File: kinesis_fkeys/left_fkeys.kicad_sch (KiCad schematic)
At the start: 10 parts, among them J2 LEFT_13_TOP

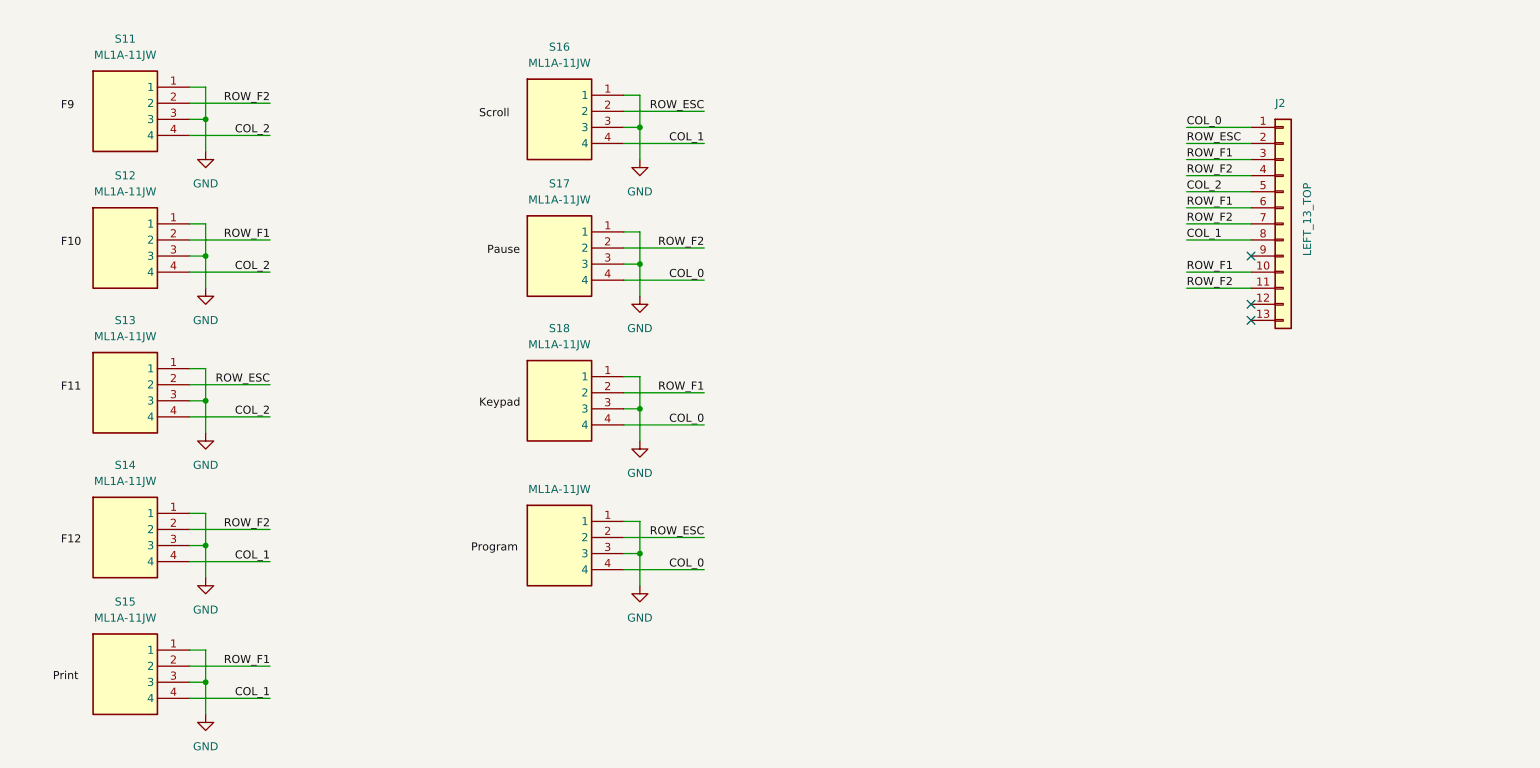
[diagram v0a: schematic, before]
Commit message: buttons schematics verified and placed on the pcb on exact spots
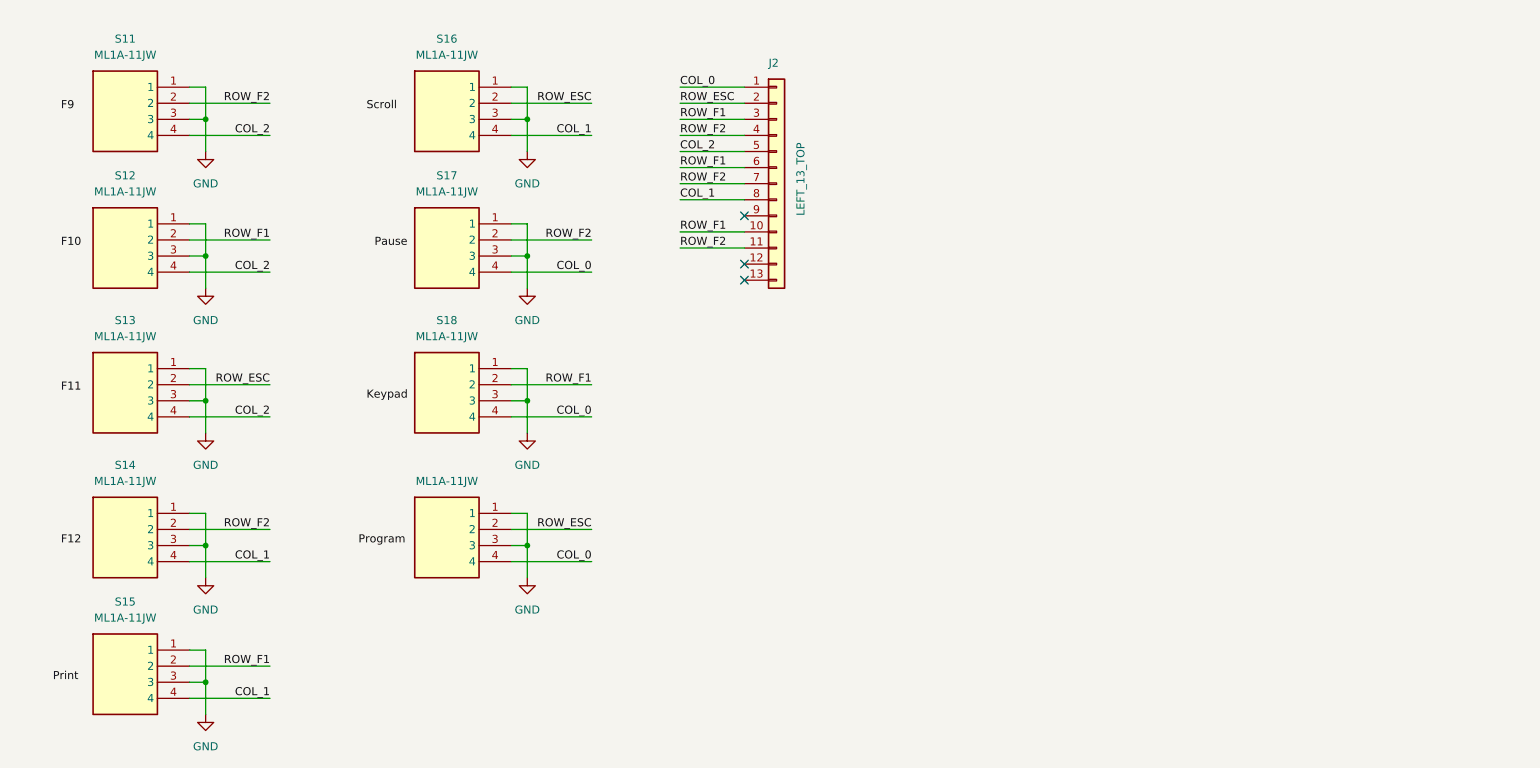
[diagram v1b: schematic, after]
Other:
- moved on the sheet: J2, S16, S17, S18

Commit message: added diods againts ghosting on the both PCBs
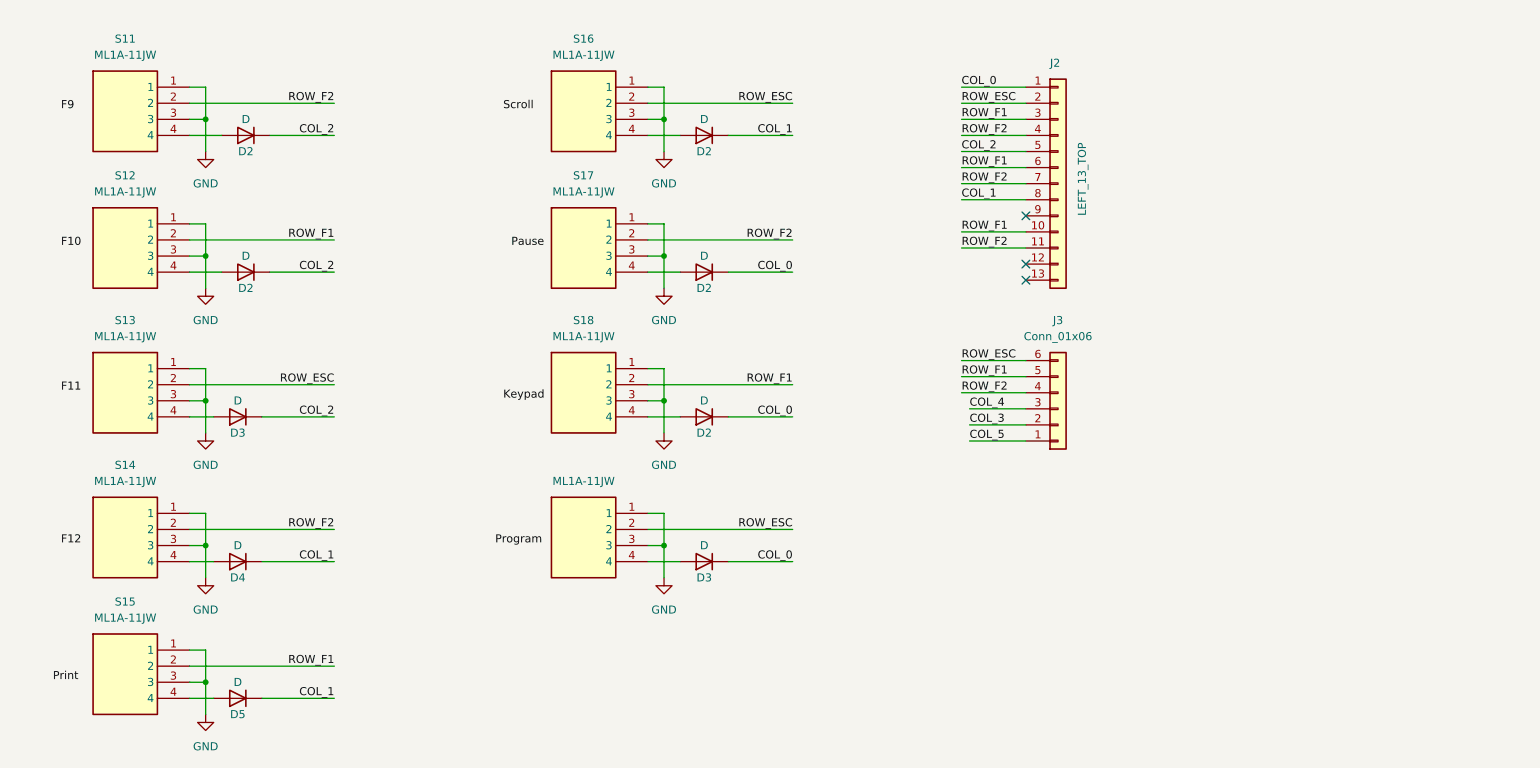
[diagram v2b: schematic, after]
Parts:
- added D2 (x5), D3 (x2), D4, D5: D, Diode_SMD:D_MiniMELF_Handsoldering, symbol Device:D
- added J3: Conn_01x06, symbol Connector_Generic:Conn_01x06
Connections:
- net COL_0: now also D2.1 (K), D2.1 (K), D3.1 (K); no longer S10.4, S17.4, S18.4
- net COL_1: now also D2.1 (K), D4.1 (K), D5.1 (K); no longer S14.4, S15.4, S16.4
- net COL_2: now also D2.1 (K), D2.1 (K), D3.1 (K); no longer S11.4, S12.4, S13.4
- net ROW_ESC: now also J3.6 (Pin_6)
- net ROW_F1: now also J3.5 (Pin_5)
- net ROW_F2: now also J3.4 (Pin_4)
- new net: D5.2 (A), S15.4
- new net: D2.2 (A), S17.4
- new net: D4.2 (A), S14.4
- new net: D3.2 (A), S13.4
- new net: D2.2 (A), S16.4
- new net: D2.2 (A), S11.4
- new net: D2.2 (A), S12.4
- new net: D2.2 (A), S18.4
- new net: D3.2 (A), S10.4
- new net COL_3: J3.2 (Pin_2)
- new net COL_4: J3.3 (Pin_3)
- new net COL_5: J3.1 (Pin_1)
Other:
- moved on the sheet: J2, S16, S17, S18

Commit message: added TE 84953 6 pin connectors to reduce amount of tracks
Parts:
- J3: footprint (none) -> dodo_conn:84953-6
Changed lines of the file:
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@@
       (effects (font (size 1.27 1.27)))
     )
-    (property "Footprint" "" (at 200.66 87.63 0)
+    (property "Footprint" "dodo_conn:84953-6" (at 200.66 87.63 0)
       (effects (font (size 1.27 1.27)) hide)
     )

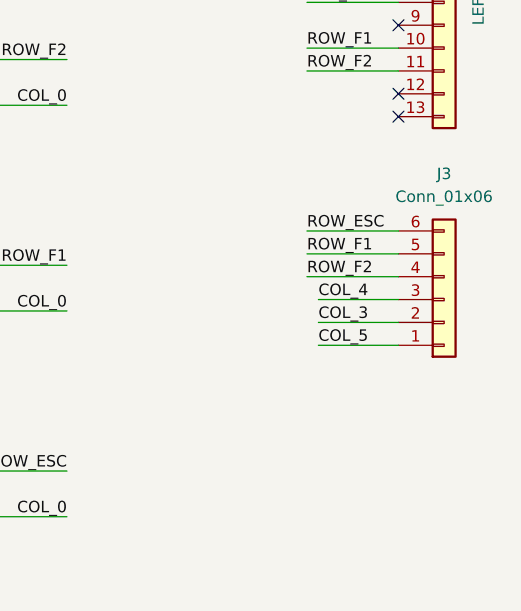
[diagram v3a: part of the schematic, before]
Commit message: fixed wrong amount pins on the footprint and sorted pinout on the connectors
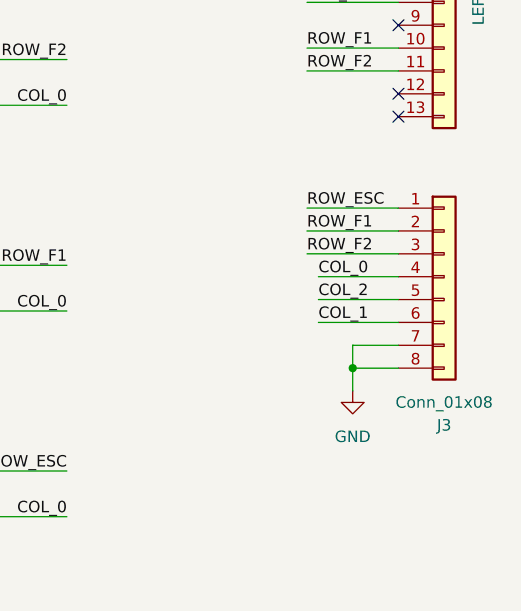
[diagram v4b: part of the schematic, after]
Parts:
- removed J3: Conn_01x06, dodo_conn:84953-6, symbol Connector_Generic:Conn_01x06
- added J3: Conn_01x08, dodo_conn:84953-6, symbol Connector_Generic:Conn_01x08
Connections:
- net COL_0: now also J3.4 (Pin_4)
- net COL_1: now also J3.6 (Pin_6)
- net COL_2: now also J3.5 (Pin_5)
- net GND: now also J3.7 (Pin_7), J3.8 (Pin_8)
- net ROW_ESC: now also J3.1 (Pin_1)
- net ROW_F1: now also J3.2 (Pin_2)
- net ROW_F2: now also J3.3 (Pin_3)
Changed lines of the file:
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@@
   (junction (at 66.04 41.91) (diameter 0) (color 0 0 0 0)
+  )
+  (junction (at 190.5 95.25) (diameter 0) (color 0 0 0 0)
   )
   (junction (at 66.04 63.5) (diameter 0) (color 0 0 0 0)
@@
     (stroke (width 0) (type default))
   )
+  (wire (pts (xy 185.42 80.01) (xy 195.58 80.01))
+    (stroke (width 0) (type default))
+  )
   (wire (pts (xy 66.04 36.83) (xy 66.04 41.91))
     (stroke (width 0) (type default))
@@
     (stroke (width 0) (type default))
   )
+  (wire (pts (xy 186.69 90.17) (xy 195.58 90.17))
+    (stroke (width 0) (type default))
+  )
   (wire (pts (xy 138.43 81.28) (xy 138.43 86.36))
     (stroke (width 0) (type default))
@@
     (stroke (width 0) (type default))
   )
+  (wire (pts (xy 190.5 95.25) (xy 190.5 97.79))
+    (stroke (width 0) (type default))
+  )
   (wire (pts (xy 66.04 41.91) (xy 66.04 46.99))
     (stroke (width 0) (type default))
@@
     (stroke (width 0) (type default))
   )
+  (wire (pts (xy 186.69 85.09) (xy 195.58 85.09))
+    (stroke (width 0) (type default))
+  )
   (wire (pts (xy 138.43 86.36) (xy 138.43 91.44))
     (stroke (width 0) (type default))
@@
     (stroke (width 0) (type default))
   )
+  (wire (pts (xy 190.5 92.71) (xy 190.5 95.25))
+    (stroke (width 0) (type default))
+  )
   (wire (pts (xy 135.89 88.9) (xy 140.97 88.9))
     (stroke (width 0) (type default))
@@
     (stroke (width 0) (type default))
   )
-  (wire (pts (xy 195.58 92.71) (xy 186.69 92.71))
-    (stroke (width 0) (type default))
-  )
   (wire (pts (xy 138.43 63.5) (xy 138.43 68.58))
     (stroke (width 0) (type default))
@@
     (stroke (width 0) (type default))
   )
-  (wire (pts (xy 195.58 82.55) (xy 185.42 82.55))
-    (stroke (width 0) (type default))
-  )
   (wire (pts (xy 63.5 41.91) (xy 66.04 41.91))
     (stroke (width 0) (type default))
   )
+  (wire (pts (xy 185.42 77.47) (xy 195.58 77.47))
+    (stroke (width 0) (type default))
+  )
   (wire (pts (xy 148.59 66.04) (xy 158.75 66.04))
     (stroke (width 0) (type default))
@@
     (stroke (width 0) (type default))
   )
-  (wire (pts (xy 195.58 87.63) (xy 186.69 87.63))
-    (stroke (width 0) (type default))
-  )
   (wire (pts (xy 63.5 44.45) (xy 68.58 44.45))
     (stroke (width 0) (type default))
@@
     (stroke (width 0) (type default))
   )
-  (wire (pts (xy 195.58 80.01) (xy 185.42 80.01))
-    (stroke (width 0) (type default))
-  )
   (wire (pts (xy 63.5 104.14) (xy 66.04 104.14))
     (stroke (width 0) (type default))
   )
+  (wire (pts (xy 195.58 92.71) (xy 190.5 92.71))
+    (stroke (width 0) (type default))
+  )
   (wire (pts (xy 135.89 81.28) (xy 138.43 81.28))
     (stroke (width 0) (type default))
@@
     (stroke (width 0) (type default))
   )
-  (wire (pts (xy 195.58 90.17) (xy 186.69 90.17))
+  (wire (pts (xy 185.42 82.55) (xy 195.58 82.55))
     (stroke (width 0) (type default))
   )
@@
     (stroke (width 0) (type default))
   )
-  (wire (pts (xy 195.58 85.09) (xy 185.42 85.09))
-    (stroke (width 0) (type default))
-  )
   (wire (pts (xy 135.89 111.76) (xy 140.97 111.76))
     (stroke (width 0) (type default))
@@
     (stroke (width 0) (type default))
   )
+  (wire (pts (xy 195.58 95.25) (xy 190.5 95.25))
+    (stroke (width 0) (type default))
+  )
+  (wire (pts (xy 186.69 87.63) (xy 195.58 87.63))
+    (stroke (width 0) (type default))
+  )
   (wire (pts (xy 138.43 41.91) (xy 138.43 46.99))
     (stroke (width 0) (type default))
@@
     (effects (font (size 1.27 1.27)) (justify right bottom))
   )
-  (label "COL_5" (at 186.69 92.71 0) (fields_autoplaced)
+  (label "COL_1" (at 186.69 90.17 0) (fields_autoplaced)
     (effects (font (size 1.27 1.27)) (justify left bottom))
   )
@@
     (effects (font (size 1.27 1.27)) (justify left bottom))
   )
-  (label "ROW_F2" (at 185.42 85.09 0) (fields_autoplaced)
+  (label "ROW_F2" (at 185.42 82.55 0) (fields_autoplaced)
     (effects (font (size 1.27 1.27)) (justify left bottom))
   )
@@
     (effects (font (size 1.27 1.27)) (justify right bottom))
   )
-  (label "COL_3" (at 186.69 90.17 0) (fields_autoplaced)
+  (label "COL_2" (at 186.69 87.63 0) (fields_autoplaced)
     (effects (font (size 1.27 1.27)) (justify left bottom))
   )
@@
     (effects (font (size 1.27 1.27)) (justify left bottom))
   )
-  (label "ROW_F1" (at 185.42 82.55 0) (fields_autoplaced)
+  (label "ROW_F1" (at 185.42 80.01 0) (fields_autoplaced)
     (effects (font (size 1.27 1.27)) (justify left bottom))
   )
@@
     (effects (font (size 1.27 1.27)) (justify left bottom))
   )
-  (label "COL_4" (at 186.69 87.63 0) (fields_autoplaced)
-    (effects (font (size 1.27 1.27)) (justify left bottom))
-  )
-  (label "ROW_ESC" (at 185.42 80.01 0) (fields_autoplaced)
+  (label "COL_0" (at 186.69 85.09 0) (fields_autoplaced)
+    (effects (font (size 1.27 1.27)) (justify left bottom))
+  )
+  (label "ROW_ESC" (at 185.42 77.47 0) (fields_autoplaced)
     (effects (font (size 1.27 1.27)) (justify left bottom))
   )
@@
         (path "/06886ccb-17ec-482e-a853-bf4276494c0a/d08dcb93-9608-43f8-96f0-931b8e1132a9"
           (reference "D10") (unit 1)
-        )
-      )
-    )
-  )
-  (symbol (lib_id "Connector_Generic:Conn_01x06") (at 200.66 87.63 0) (mirror x) (unit 1)
-    (exclude_from_sim no) (in_bom yes) (on_board yes) (dnp no) (fields_autoplaced)
-    (property "Reference" "J3" (at 200.66 73.66 0)
-      (effects (font (size 1.27 1.27)))
-    )
-    (property "Value" "Conn_01x06" (at 200.66 76.2 0)
-      (effects (font (size 1.27 1.27)))
-    )
-    (property "Footprint" "dodo_conn:84953-6" (at 200.66 87.63 0)
-      (effects (font (size 1.27 1.27)) hide)
-    )
-    (property "Datasheet" "~" (at 200.66 87.63 0)
-      (effects (font (size 1.27 1.27)) hide)
-    )
-    (property "Description" "Generic connector, single row, 01x06, script generated (kicad-library-utils/schlib/autogen/connector/)" (at 200.66 87.63 0)
-      (effects (font (size 1.27 1.27)) hide)
-    )
-    (pin "6")
-    (pin "1")
-    (pin "2")
-    (pin "5")
-    (pin "3")
-    (pin "4")
-    (instances
-      (project "kinesis_fkeys"
-        (path "/06886ccb-17ec-482e-a853-bf4276494c0a/106b8080-7c92-4036-9b29-d3ff48894255"
-          (reference "J3") (unit 1)
-        )
-        (path "/06886ccb-17ec-482e-a853-bf4276494c0a/d08dcb93-9608-43f8-96f0-931b8e1132a9"
-          (reference "J4") (unit 1)
         )
       )
@@
     )
   )
+  (symbol (lib_id "power:GND") (at 190.5 97.79 0) (mirror y) (unit 1)
+    (exclude_from_sim no) (in_bom yes) (on_board yes) (dnp no) (fields_autoplaced)
+    (property "Reference" "#PWR019" (at 190.5 104.14 0)
+      (effects (font (size 1.27 1.27)) hide)
+    )
+    (property "Value" "GND" (at 190.5 102.87 0)
+      (effects (font (size 1.27 1.27)))
+    )
+    (property "Footprint" "" (at 190.5 97.79 0)
+      (effects (font (size 1.27 1.27)) hide)
+    )
+    (property "Datasheet" "" (at 190.5 97.79 0)
+      (effects (font (size 1.27 1.27)) hide)
+    )
+    (property "Description" "Power symbol creates a global label with name \"GND\" , ground" (at 190.5 97.79 0)
+      (effects (font (size 1.27 1.27)) hide)
+    )
+    (pin "1")
+    (instances
+      (project "kinesis_fkeys"
+        (path "/06886ccb-17ec-482e-a853-bf4276494c0a/106b8080-7c92-4036-9b29-d3ff48894255"
+          (reference "#PWR019") (unit 1)
+        )
+        (path "/06886ccb-17ec-482e-a853-bf4276494c0a/d08dcb93-9608-43f8-96f0-931b8e1132a9"
+          (reference "#PWR020") (unit 1)
+        )
+      )
+    )
+  )
   (symbol (lib_id "power:GND") (at 66.04 68.58 0) (unit 1)
     (exclude_from_sim no) (in_bom yes) (on_board yes) (dnp no) (fields_autoplaced)
@@
         )
       )
+    )
+  )
+  (symbol (lib_id "Connector_Generic:Conn_01x08") (at 200.66 85.09 0) (unit 1)
+    (exclude_from_sim no) (in_bom yes) (on_board yes) (dnp no)
+    (property "Reference" "J3" (at 200.66 101.6 0)
+      (effects (font (size 1.27 1.27)))
+    )
+    (property "Value" "Conn_01x08" (at 200.66 99.06 0)
+      (effects (font (size 1.27 1.27)))
+    )
+    (property "Footprint" "dodo_conn:84953-6" (at 200.66 85.09 0)
+      (effects (font (size 1.27 1.27)) hide)
+    )
+    (property "Datasheet" "~" (at 200.66 85.09 0)
+      (effects (font (size 1.27 1.27)) hide)
+    )
+    (property "Description" "Generic connector, single row, 01x08, script generated (kicad-library-utils/schlib/autogen/connector/)" (at 200.66 85.09 0)
+      (effects (font (size 1.27 1.27)) hide)
+    )
+    (pin "2")
+    (pin "1")
+    (pin "4")
+    (pin "6")
+    (pin "3")
+    (pin "8")
+    (pin "7")
+    (pin "5")
+    (instances
+      (project "kinesis_fkeys"
+        (path "/06886ccb-17ec-482e-a853-bf4276494c0a/106b8080-7c92-4036-9b29-d3ff48894255"
+          (reference "J3") (unit 1)
+        )
+        (path "/06886ccb-17ec-482e-a853-bf4276494c0a/d08dcb93-9608-43f8-96f0-931b8e1132a9"
+          (reference "J5") (unit 1)
+        )
+      )

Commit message: positioning of components and added filled zones
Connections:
- net GND: no longer J3.7 (Pin_7), J3.8 (Pin_8), S10.1, S10.3, S11.1, S11.3, S13.1, S13.3, S14.1, S14.3, S15.1, S15.3, S16.1, S16.3, S17.1, S17.3, S18.1, S18.3
- new net GND_L: J3.7 (Pin_7), J3.8 (Pin_8), S10.1, S10.3, S11.1, S11.3, S13.1, S13.3, S14.1, S14.3, S15.1, S15.3, S16.1, S16.3, S17.1, S17.3, S18.1, S18.3
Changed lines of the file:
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@@
       (effects (font (size 1.27 1.27)) hide)
     )
-    (property "Value" "GND" (at 138.43 119.38 0)
+    (property "Value" "GND_L" (at 138.43 119.38 0)
       (effects (font (size 1.27 1.27)))
     )
@@
       (effects (font (size 1.27 1.27)) hide)
     )
-    (property "Value" "GND" (at 138.43 52.07 0)
+    (property "Value" "GND_L" (at 138.43 52.07 0)
       (effects (font (size 1.27 1.27)))
     )
@@
       (effects (font (size 1.27 1.27)) hide)
     )
-    (property "Value" "GND" (at 66.04 52.07 0)
+    (property "Value" "GND_L" (at 66.04 52.07 0)
       (effects (font (size 1.27 1.27)))
     )
@@
       (effects (font (size 1.27 1.27)) hide)
     )
-    (property "Value" "GND" (at 66.04 96.52 0)
+    (property "Value" "GND_L" (at 66.04 96.52 0)
       (effects (font (size 1.27 1.27)))
     )
@@
       (effects (font (size 1.27 1.27)) hide)
     )
-    (property "Value" "GND" (at 138.43 96.52 0)
+    (property "Value" "GND_L" (at 138.43 96.52 0)
       (effects (font (size 1.27 1.27)))
     )
@@
       (effects (font (size 1.27 1.27)) hide)
     )
-    (property "Value" "GND" (at 138.43 73.66 0)
+    (property "Value" "GND_L" (at 138.43 73.66 0)
       (effects (font (size 1.27 1.27)))
     )
@@
       (effects (font (size 1.27 1.27)) hide)
     )
-    (property "Value" "GND" (at 66.04 140.97 0)
+    (property "Value" "GND_L" (at 66.04 140.97 0)
       (effects (font (size 1.27 1.27)))
     )
@@
       (effects (font (size 1.27 1.27)) hide)
     )
-    (property "Value" "GND" (at 66.04 119.38 0)
+    (property "Value" "GND_L" (at 66.04 119.38 0)
       (effects (font (size 1.27 1.27)))
     )
@@
       (effects (font (size 1.27 1.27)) hide)
     )
-    (property "Value" "GND" (at 190.5 102.87 0)
-      (effects (font (size 1.27 1.27)))
-    )
+    (property "Value" "GND_L" (at 190.5 102.87 0)
+      (effects (font (size 1.27 1.27)))
+    )
